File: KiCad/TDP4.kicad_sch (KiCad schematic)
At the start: 4 parts, among them J1 MD240128A6W-FPTLW, U1 Pico

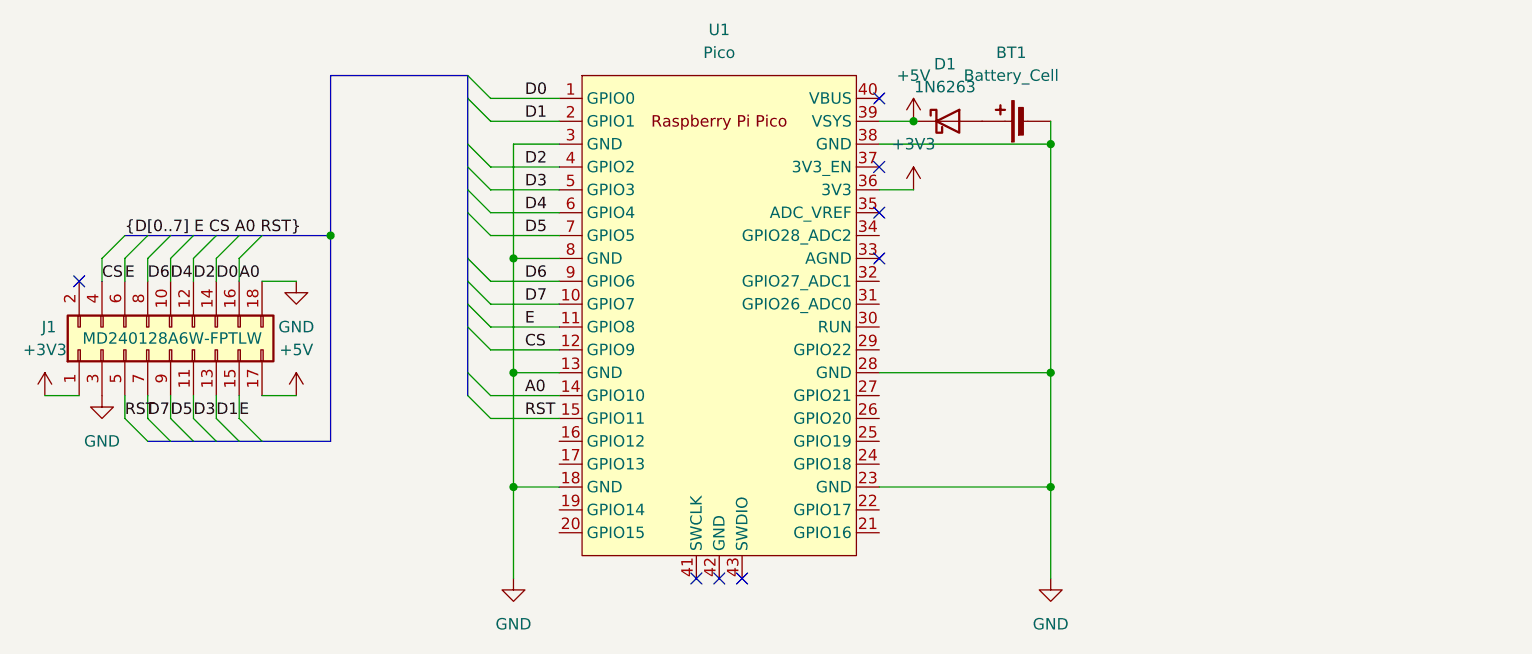
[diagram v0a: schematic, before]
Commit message: Updated KiCad model
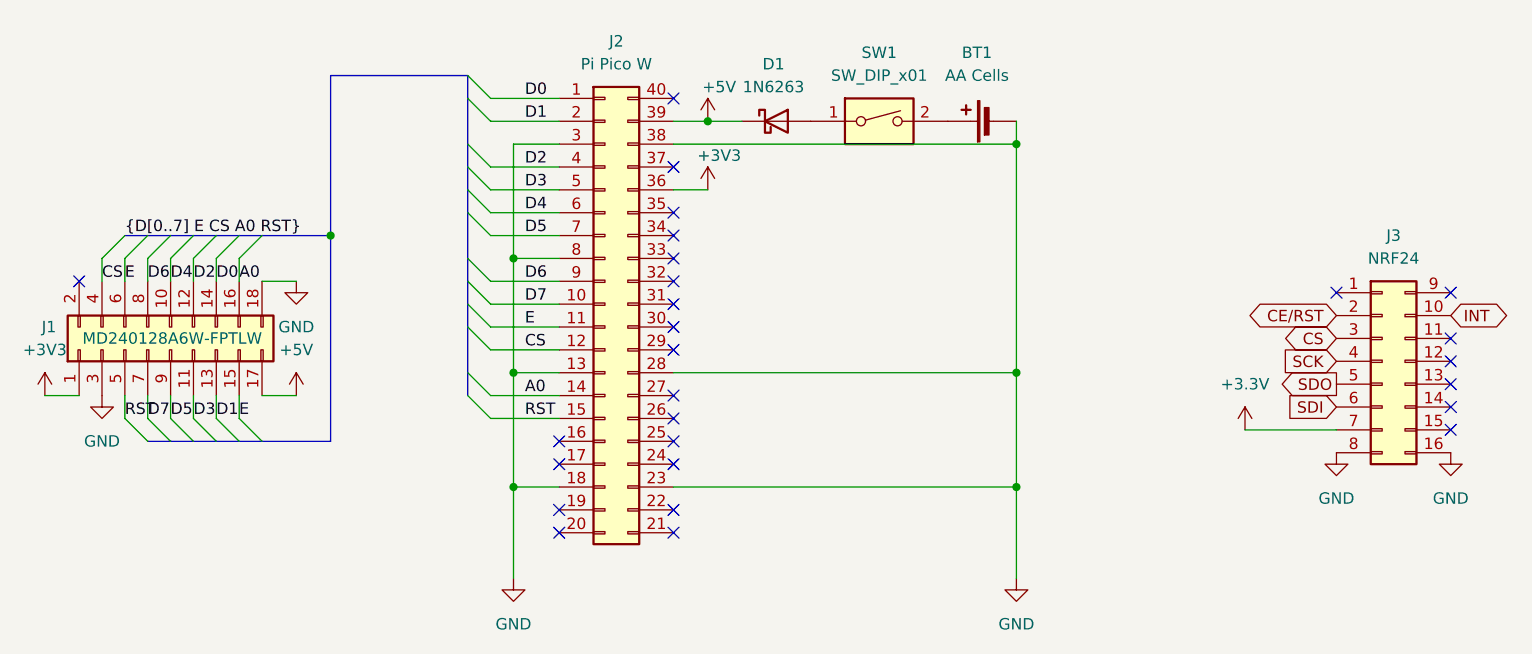
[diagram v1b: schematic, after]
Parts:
- removed U1: Pico, RPi_Pico:RPi_Pico_SMD_TH, symbol MCU_RaspberryPi_and_Boards:Pico
- added J2: Pi Pico W, symbol Connector_Generic:Conn_02x20_Counter_Clockwise
- added J3: NRF24, symbol Connector_Generic:Conn_02x08_Top_Bottom
- added SW1: SW_DIP_x01, symbol Switch:SW_DIP_x01
- BT1: value Battery_Cell -> AA Cells
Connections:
- net +3V3: now also J2.36 (Pin_36)
- net +5V: now also J2.39 (Pin_39)
- net A0: now also J2.14 (Pin_14)
- net CS: now also J2.12 (Pin_12), J3.3 (Pin_3)
- net D0: now also J2.1 (Pin_1)
- net D1: now also J2.2 (Pin_2)
- net D2: now also J2.4 (Pin_4)
- net D3: now also J2.5 (Pin_5)
- net D4: now also J2.6 (Pin_6)
- net D5: now also J2.7 (Pin_7)
- net D6: now also J2.9 (Pin_9)
- net D7: now also J2.10 (Pin_10)
- net E: now also J2.11 (Pin_11)
- net GND: now also J2.13 (Pin_13), J2.18 (Pin_18), J2.23 (Pin_23), J2.28 (Pin_28), J2.3 (Pin_3), J2.38 (Pin_38), J2.8 (Pin_8), J3.16 (Pin_16), J3.8 (Pin_8)
- net RST: now also J2.15 (Pin_15)
- net at D1.2 (A): now also SW1.1; no longer BT1.1 (+)
- new net: BT1.1 (+), SW1.2
- new net +3.3V: J3.7 (Pin_7)
- new net CE/RST: J3.2 (Pin_2)
- new net INT: J3.10 (Pin_10)
- new net SCK: J3.4 (Pin_4)
- new net SDI: J3.6 (Pin_6)
- new net SDO: J3.5 (Pin_5)
- no-connect marks 8 -> 27
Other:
- moved on the sheet: BT1, D1
